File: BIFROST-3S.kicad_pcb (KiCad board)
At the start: 4 copper layers, 46 x 23 mm, 14 parts, among them J1 B6B-XH-A_LF__SN_, J2 Conn_01x12, J3 B4B-XH-A_LF__SN_, J4 XT30PW-M

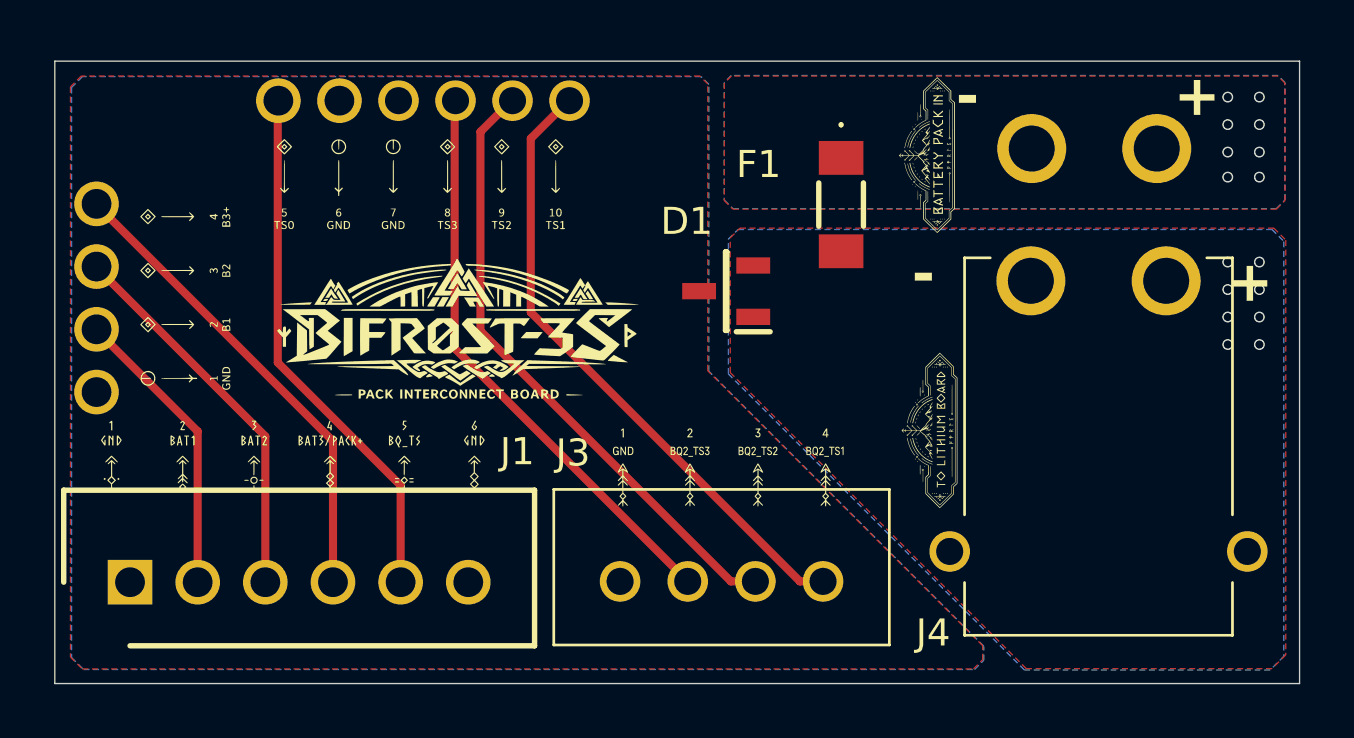
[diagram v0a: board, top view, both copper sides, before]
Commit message: Fixed Vias+Pins
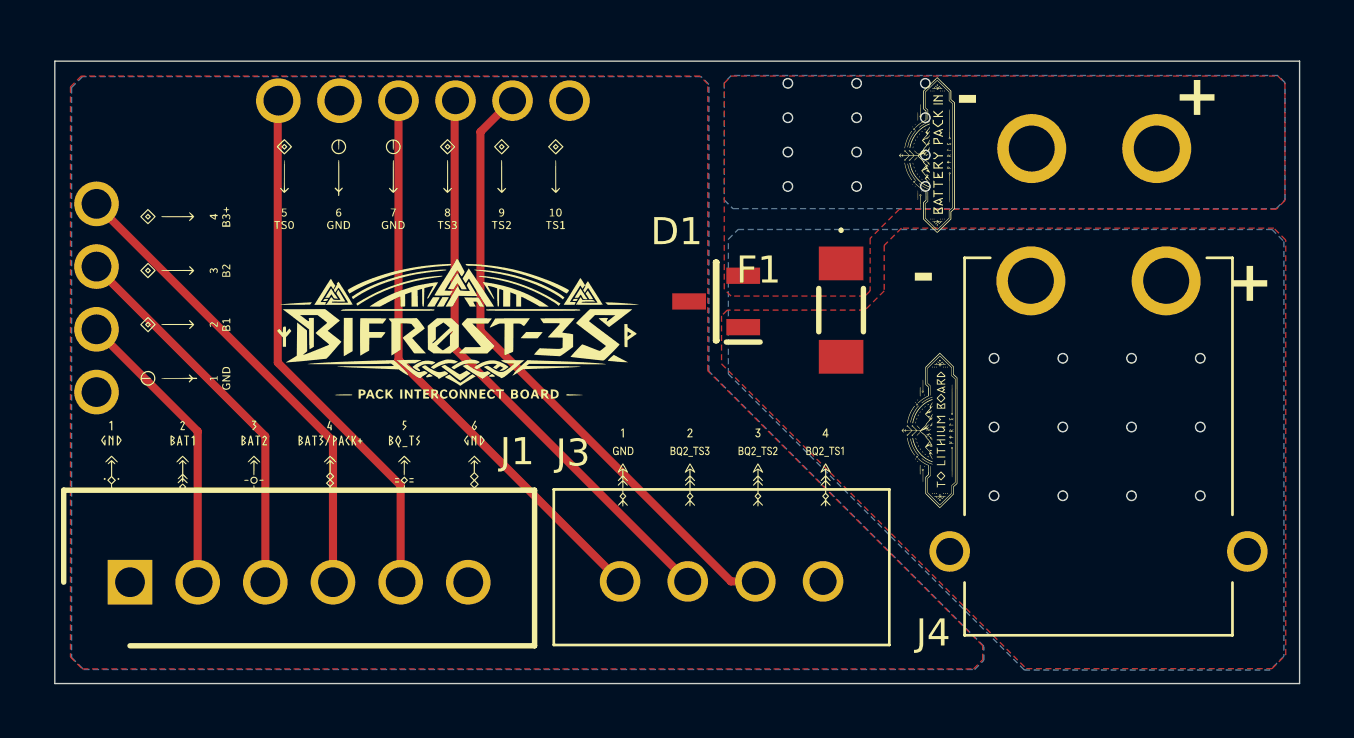
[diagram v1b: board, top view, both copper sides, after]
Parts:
- moved F1 3.90 mm to (151.8, 107.4)
- moved D1 0.53 mm to (147.2, 107.1)
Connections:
- J2 pad 10: /BQ2_TS1 -> GND
- J2 pad 7: GND -> /BQ2_TS1
- J2 pad 8: /BQ2_TS3 -> /BQ2_TS2
- J2 pad 9: /BQ2_TS2 -> /BQ2_TS3
- J3 pad 1: GND -> /BQ2_TS1
- J3 pad 2: /BQ2_TS3 -> /BQ2_TS2
- J3 pad 3: /BQ2_TS2 -> /BQ2_TS3
- J3 pad 4: /BQ2_TS1 -> GND
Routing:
- net /BQ2_TS1: track 23.3 -> 21.2 mm
- net /BQ2_TS3: track 21.3 -> 23.0 mm
- net /BQ2_TS2: track 23.0 -> 21.3 mm
- net /PACK+_RAW: vias 8 -> 12
- net /+BATT: vias 8 -> 12
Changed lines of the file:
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@@
 	(footprint "SF-1206HHA800R-2:SF1206HHA800R2"
 		(layer "F.Cu")
-		(at 151.8275 103.54 -90)
+		(at 151.8275 107.44 -90)
 		(descr "SF-1206HHA800R-2")
 		(tags "Fuse")
@@
 			(layers "*.Cu" "*.Mask")
 			(remove_unused_layers no)
-			(net 1 "GND")
+			(net 5 "/BQ2_TS1")
 			(pinfunction "1")
 			(pintype "passive")
@@
 			(layers "*.Cu" "*.Mask")
 			(remove_unused_layers no)
-			(net 10 "/BQ2_TS3")
+			(net 9 "/BQ2_TS2")
 			(pinfunction "2")
 			(pintype "passive")
@@
 			(layers "*.Cu" "*.Mask")
 			(remove_unused_layers no)
-			(net 9 "/BQ2_TS2")
+			(net 10 "/BQ2_TS3")
 			(pinfunction "3")
 			(pintype "passive")
@@
 			(layers "*.Cu" "*.Mask")
 			(remove_unused_layers no)
-			(net 5 "/BQ2_TS1")
+			(net 1 "GND")
 			(pinfunction "4")
 			(pintype "passive")
@@
 			(layers "*.Cu" "*.Mask")
 			(remove_unused_layers no)
-			(net 1 "GND")
+			(net 5 "/BQ2_TS1")
 			(pinfunction "Pin_7")
 			(pintype "passive")
@@
 			(layers "*.Cu" "*.Mask")
 			(remove_unused_layers no)
-			(net 10 "/BQ2_TS3")
+			(net 9 "/BQ2_TS2")
 			(pinfunction "Pin_8")
 			(pintype "passive")
@@
 			(layers "*.Cu" "*.Mask")
 			(remove_unused_layers no)
-			(net 9 "/BQ2_TS2")
+			(net 10 "/BQ2_TS3")
 			(pinfunction "Pin_9")
 			(pintype "passive")
@@
 			(layers "*.Cu" "*.Mask")
 			(remove_unused_layers no)
-			(net 5 "/BQ2_TS1")
+			(net 1 "GND")
 			(pinfunction "Pin_10")
 			(pintype "passive")
@@
 	(footprint "CDSOT23-T15C-Q:SOT95P230X117-3N"
 		(layer "F.Cu")
-		(at 147.58 106.74 180)
+		(at 147.21 107.12 180)
 		(descr "SOT-323_2021")
 		(tags "TVS Diode (Bi-directional)")
@@
 	)
 	(via
-		(at 167.284 108.712)
+		(at 157.48 111.76)
+		(size 0.4)
+		(drill 0.3)
+		(layers "F.Cu" "B.Cu")
+		(free yes)
+		(tenting front back)
+		(net 3)
+	)
+	(via
+		(at 162.56 114.3)
+		(size 0.4)
+		(drill 0.3)
+		(layers "F.Cu" "B.Cu")
+		(free yes)
+		(tenting front back)
+		(net 3)
+	)
+	(via
+		(at 162.56 109.22)
 		(size 0.4)
 		(drill 0.3)
@@
 	)
 	(via
-		(at 166.116 106.68)
+		(at 160.02 109.22)
 		(size 0.4)
 		(drill 0.3)
@@
 	)
 	(via
-		(at 166.116 107.696)
+		(at 160.02 111.76)
 		(size 0.4)
 		(drill 0.3)
@@
 	)
 	(via
-		(at 167.284 107.696)
+		(at 157.48 109.22)
 		(size 0.4)
 		(drill 0.3)
@@
 	)
 	(via
-		(at 166.116 108.712)
+		(at 165.1 114.3)
 		(size 0.4)
 		(drill 0.3)
@@
 	)
 	(via
-		(at 167.284 105.664)
+		(at 165.1 111.76)
 		(size 0.4)
 		(drill 0.3)
@@
 	)
 	(via
-		(at 166.116 105.664)
+		(at 165.1 109.22)
 		(size 0.4)
 		(drill 0.3)
@@
 	)
 	(via
-		(at 167.284 106.68)
+		(at 160.02 114.3)
+		(size 0.4)
+		(drill 0.3)
+		(layers "F.Cu" "B.Cu")
+		(free yes)
+		(tenting front back)
+		(net 3)
+	)
+	(via
+		(at 162.56 111.76)
+		(size 0.4)
+		(drill 0.3)
+		(layers "F.Cu" "B.Cu")
+		(free yes)
+		(tenting front back)
+		(net 3)
+	)
+	(via
+		(at 157.48 114.3)
 		(size 0.4)
 		(drill 0.3)
@@
 	)
 	(segment
-		(start 140.36 107.52)
-		(end 150.305 117.465)
+		(start 135.471 109.276)
+		(end 143.66 117.465)
 		(width 0.3)
 		(layer "F.Cu")
@@
 	)
 	(segment
-		(start 141.76 99.7)
-		(end 140.36 101.1)
+		(start 135.471 99.7)
+		(end 135.471 109.276)
 		(width 0.3)
 		(layer "F.Cu")
 		(net 5)
 	)
-	(segment
-		(start 140.36 101.1)
-		(end 140.36 107.52)
-		(width 0.3)
-		(layer "F.Cu")
-		(net 5)
+	(via
+		(at 152.4 100.33)
+		(size 0.4)
+		(drill 0.3)
+		(layers "F.Cu" "B.Cu")
+		(free yes)
+		(tenting front back)
+		(net 6)
 	)
-	(segment
-		(start 150.305 117.465)
-		(end 151.16 117.465)
-		(width 0.3)
-		(layer "F.Cu")
-		(net 5)
+	(via
+		(at 154.94 102.87)
+		(size 0.4)
+		(drill 0.3)
+		(layers "F.Cu" "B.Cu")
+		(free yes)
+		(tenting front back)
+		(net 6)
+	)
+	(via
+		(at 154.94 100.33)
+		(size 0.4)
+		(drill 0.3)
+		(layers "F.Cu" "B.Cu")
+		(free yes)
+		(tenting front back)
+		(net 6)
+	)
+	(via
+		(at 149.86 102.87)
+		(size 0.4)
+		(drill 0.3)
+		(layers "F.Cu" "B.Cu")
+		(free yes)
+		(tenting front back)
+		(net 6)
 	)
 	(via
-		(at 167.284 99.568)
+		(at 152.4 99.06)
 		(size 0.4)
 		(drill 0.3)
@@
 	)
 	(via
-		(at 166.116 101.6)
+		(at 149.86 99.06)
 		(size 0.4)
 		(drill 0.3)
@@
 	)
 	(via
-		(at 166.116 100.584)
+		(at 149.86 100.33)
 		(size 0.4)
 		(drill 0.3)
@@
 	)
 	(via
-		(at 166.116 102.525)
+		(at 152.4 102.87)
 		(size 0.4)
 		(drill 0.3)
@@
 	)
 	(via
-		(at 167.284 102.525)
+		(at 154.94 101.71)
 		(size 0.4)
 		(drill 0.3)
@@
 	)
 	(via
-		(at 167.284 100.584)
+		(at 152.4 101.6)
 		(size 0.4)
 		(drill 0.3)
@@
 	)
 	(via
-		(at 167.284 101.6)
+		(at 149.86 101.6)
 		(size 0.4)
 		(drill 0.3)
@@
 	)
 	(via
-		(at 166.116 99.568)
+		(at 154.94 99.06)
 		(size 0.4)
 		(drill 0.3)
@@
 	)
 	(segment
-		(start 138.5 108.21)
-		(end 147.755 117.465)
+		(start 137.546 108.851)
+		(end 146.16 117.465)
 		(width 0.3)
 		(layer "F.Cu")
@@
 	)
 	(segment
-		(start 147.755 117.465)
-		(end 148.66 117.465)
+		(start 137.546 99.7)
+		(end 137.546 108.851)
 		(width 0.3)
 		(layer "F.Cu")
@@
 	)
 	(segment
-		(start 139.653 99.7)
-		(end 138.5 100.853)
+		(start 138.5 108.21)
+		(end 147.755 117.465)
 		(width 0.3)
 		(layer "F.Cu")
-		(net 9)
+		(net 10)
 	)
 	(segment
-		(start 138.5 100.853)
-		(end 138.5 108.21)
+		(start 147.755 117.465)
+		(end 148.66 117.465)
 		(width 0.3)
 		(layer "F.Cu")
-		(net 9)
+		(net 10)
 	)
 	(segment
-		(start 137.546 108.851)
-		(end 146.16 117.465)
+		(start 139.653 99.7)
+		(end 138.5 100.853)
 		(width 0.3)
 		(layer "F.Cu")
@@
 	)
 	(segment
-		(start 137.546 99.7)
-		(end 137.546 108.851)
+		(start 138.5 100.853)
+		(end 138.5 108.21)
 		(width 0.3)
 		(layer "F.Cu")
@@
 	)
 	(zone
-		(net 1)
-		(net_name "GND")
+		(net 6)
+		(net_name "/PACK+_RAW")
 		(layer "F.Cu")
 		(hatch edge 0.5)
-		(priority 3)
+		(priority 5)
 		(connect_pads yes
 			(clearance 0.5)
@@
 		(polygon
 			(pts
-				(xy 123.35 120.26) (xy 123.79 120.7) (xy 156.72 120.7) (xy 157.06 120.36) (xy 157.06 119.84) (xy 146.9 109.68)
-				(xy 146.9 99.08) (xy 146.61 98.79) (xy 123.75 98.79) (xy 123.35 99.19)
+				(xy 167.91 103.71) (xy 153.98 103.71) (xy 152.9 104.79) (xy 152.9 106.73) (xy 152.71 106.92) (xy 147.76 106.92)
+				(xy 147.51 106.67) (xy 147.51 99.05) (xy 147.77 98.79) (xy 167.97 98.79) (xy 168.23 99.05) (xy 168.23 103.39)
 			)
 		)
 	)
 	(zone
-		(net 6)
-		(net_name "/PACK+_RAW")
+		(net 1)
+		(net_name "GND")
 		(layer "F.Cu")
 		(hatch edge 0.5)
+		(priority 3)
 		(connect_pads yes
 			(clearance 0.5)
@@
 		(polygon
 			(pts
-				(xy 147.83 103.71) (xy 167.91 103.71) (xy 168.23 103.39) (xy 168.23 99.05) (xy 167.97 98.79) (xy 147.77 98.79)
-				(xy 147.51 99.05) (xy 147.51 103.39)
+				(xy 123.35 120.26) (xy 123.79 120.7) (xy 156.72 120.7) (xy 157.06 120.36) (xy 157.06 119.84) (xy 146.9 109.68)
+				(xy 146.9 99.08) (xy 146.61 98.79) (xy 123.75 98.79) (xy 123.35 99.19)
 			)
 		)
@@
 		(layer "F.Cu")
 		(hatch edge 0.5)
-		(priority 2)
+		(priority 4)
 		(connect_pads yes
 			(clearance 0.5)
@@
 		(polygon
 			(pts
-				(xy 148.09 104.41) (xy 167.82 104.41) (xy 168.26 104.85) (xy 168.26 120.18) (xy 167.75 120.69) (xy 158.67 120.69)
-				(xy 147.73 109.75) (xy 147.73 104.77)
+				(xy 167.82 104.41) (xy 154.06 104.41) (xy 153.42 105.05) (xy 153.42 106.73) (xy 152.71 107.44) (xy 147.62 107.44)
+				(xy 147.41 107.65) (xy 147.41 109.43) (xy 158.67 120.69) (xy 167.75 120.69) (xy 168.26 120.18) (xy 168.26 104.85)
 			)
 		)
